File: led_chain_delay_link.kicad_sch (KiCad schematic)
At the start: 5 parts, among them Q2801 2N7002

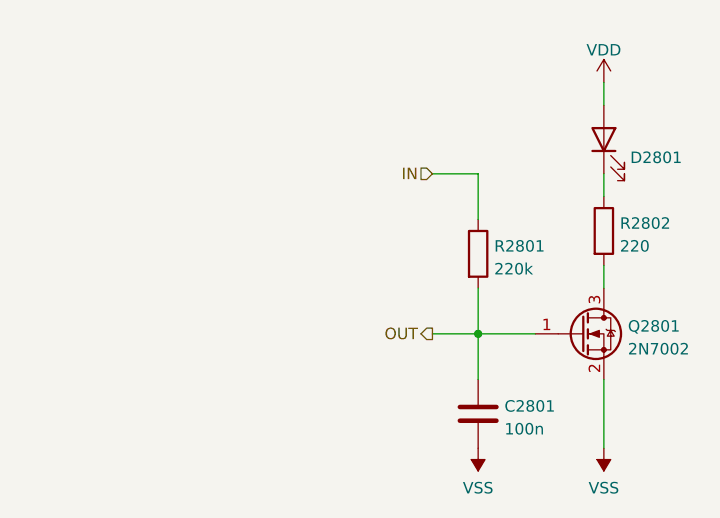
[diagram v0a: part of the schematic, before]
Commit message: sim for LED timings with gate in between
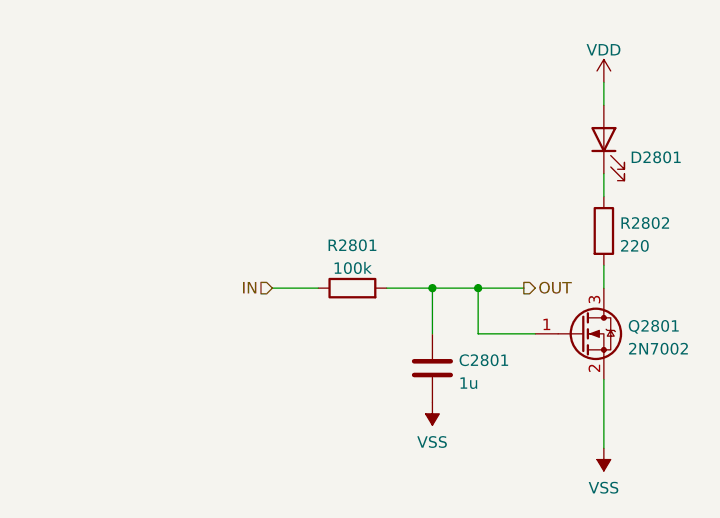
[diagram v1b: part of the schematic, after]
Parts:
- C2801: value 100n -> 1u; JLC C1525 -> C52923
- R2801: value 220k -> 100k; JLC C25767 -> C25741
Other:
- moved on the sheet: C2801, R2801
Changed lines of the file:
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@@
 (kicad_sch (version 20211123) (generator eeschema)
   (paper "A4")
-  (junction (at 146.05 172.72) (diameter 0) (color 0 0 0 0)
+  (junction (at 146.05 167.64) (diameter 0) (color 0 0 0 0)
+  )
+  (junction (at 140.97 167.64) (diameter 0) (color 0 0 0 0)
   )
   (wire (pts (xy 160.02 177.8) (xy 160.02 185.42))
+    (stroke (width 0) (type default) (color 0 0 0 0))
+  )
+  (wire (pts (xy 151.13 167.64) (xy 146.05 167.64))
+    (stroke (width 0) (type default) (color 0 0 0 0))
+  )
+  (wire (pts (xy 160.02 165.1) (xy 160.02 167.64))
     (stroke (width 0) (type default) (color 0 0 0 0))
   )
@@
     (stroke (width 0) (type default) (color 0 0 0 0))
   )
-  (wire (pts (xy 160.02 165.1) (xy 160.02 167.64))
+  (wire (pts (xy 160.02 144.78) (xy 160.02 147.32))
     (stroke (width 0) (type default) (color 0 0 0 0))
   )
-  (wire (pts (xy 160.02 144.78) (xy 160.02 147.32))
+  (wire (pts (xy 140.97 167.64) (xy 135.89 167.64))
     (stroke (width 0) (type default) (color 0 0 0 0))
   )
@@
     (stroke (width 0) (type default) (color 0 0 0 0))
   )
-  (wire (pts (xy 146.05 154.94) (xy 146.05 160.02))
+  (wire (pts (xy 146.05 167.64) (xy 140.97 167.64))
     (stroke (width 0) (type default) (color 0 0 0 0))
   )
-  (wire (pts (xy 140.97 172.72) (xy 146.05 172.72))
+  (wire (pts (xy 140.97 167.64) (xy 140.97 172.72))
     (stroke (width 0) (type default) (color 0 0 0 0))
   )
-  (wire (pts (xy 146.05 177.8) (xy 146.05 172.72))
-    (stroke (width 0) (type default) (color 0 0 0 0))
-  )
-  (wire (pts (xy 140.97 154.94) (xy 146.05 154.94))
+  (wire (pts (xy 123.19 167.64) (xy 128.27 167.64))
     (stroke (width 0) (type default) (color 0 0 0 0))
   )
@@
     (effects (font (size 2.54 2.54) (thickness 0.508) bold) (justify left bottom))
   )
-  (hierarchical_label "OUT" (shape output) (at 140.97 172.72 180)
+  (hierarchical_label "OUT" (shape output) (at 151.13 167.64 0)
+    (effects (font (size 1.27 1.27)) (justify left))
+  )
+  (hierarchical_label "IN" (shape input) (at 123.19 167.64 180)
     (effects (font (size 1.27 1.27)) (justify right))
   )
-  (hierarchical_label "IN" (shape input) (at 140.97 154.94 180)
-    (effects (font (size 1.27 1.27)) (justify right))
-  )
-  (symbol (lib_id "Device:R") (at 146.05 163.83 0) (unit 1)
+  (symbol (lib_id "Device:R") (at 132.08 167.64 90) (unit 1)
     (in_bom yes) (on_board yes) (fields_autoplaced)
-    (property "Reference" "R2801" (id 0) (at 147.828 162.9953 0)
-      (effects (font (size 1.27 1.27)) (justify left))
-    )
-    (property "Value" "220k" (id 1) (at 147.828 165.5322 0)
-      (effects (font (size 1.27 1.27)) (justify left))
-    )
-    (property "Footprint" "Resistor_SMD:R_0402_1005Metric" (id 2) (at 144.272 163.83 90)
+    (property "Reference" "R2801" (id 0) (at 132.08 162.9242 90))
+    (property "Value" "100k" (id 1) (at 132.08 165.4611 90))
+    (property "Footprint" "Resistor_SMD:R_0402_1005Metric" (id 2) (at 132.08 169.418 90)
       (effects (font (size 1.27 1.27)) hide)
     )
-    (property "Datasheet" "~" (id 3) (at 146.05 163.83 0)
+    (property "Datasheet" "~" (id 3) (at 132.08 167.64 0)
       (effects (font (size 1.27 1.27)) hide)
     )
-    (property "JLC" "C25767" (id 4) (at 146.05 163.83 90)
+    (property "JLC" "C25741" (id 4) (at 132.08 167.64 90)
       (effects (font (size 1.27 1.27)) hide)
     )
@@
     (pin "2")
   )
-  (symbol (lib_id "power:VSS") (at 146.05 185.42 180) (unit 1)
+  (symbol (lib_id "power:VSS") (at 140.97 180.34 180) (unit 1)
     (in_bom yes) (on_board yes) (fields_autoplaced)
-    (property "Reference" "#PWR02801" (id 0) (at 146.05 181.61 0)
+    (property "Reference" "#PWR02801" (id 0) (at 140.97 176.53 0)
       (effects (font (size 1.27 1.27)) hide)
     )
-    (property "Value" "VSS" (id 1) (at 146.05 189.8634 0))
-    (property "Footprint" "" (id 2) (at 146.05 185.42 0)
+    (property "Value" "VSS" (id 1) (at 140.97 184.7834 0))
+    (property "Footprint" "" (id 2) (at 140.97 180.34 0)
       (effects (font (size 1.27 1.27)) hide)
     )
-    (property "Datasheet" "" (id 3) (at 146.05 185.42 0)
+    (property "Datasheet" "" (id 3) (at 140.97 180.34 0)
       (effects (font (size 1.27 1.27)) hide)
     )
@@
     (pin "1")
   )
-  (symbol (lib_id "Device:C") (at 146.05 181.61 0) (unit 1)
+  (symbol (lib_id "Device:C") (at 140.97 176.53 0) (unit 1)
     (in_bom yes) (on_board yes) (fields_autoplaced)
-    (property "Reference" "C2801" (id 0) (at 148.971 180.7753 0)
+    (property "Reference" "C2801" (id 0) (at 143.891 175.6953 0)
       (effects (font (size 1.27 1.27)) (justify left))
     )
-    (property "Value" "100n" (id 1) (at 148.971 183.3122 0)
+    (property "Value" "1u" (id 1) (at 143.891 178.2322 0)
       (effects (font (size 1.27 1.27)) (justify left))
     )
-    (property "Footprint" "Capacitor_SMD:C_0402_1005Metric" (id 2) (at 147.0152 185.42 0)
+    (property "Footprint" "Capacitor_SMD:C_0402_1005Metric" (id 2) (at 141.9352 180.34 0)
       (effects (font (size 1.27 1.27)) hide)
     )
-    (property "Datasheet" "https://datasheet.lcsc.com/lcsc/1810191219_Samsung-Electro-Mechanics-CL05B104KO5NNNC_C1525.pdf" (id 3) (at 146.05 181.61 0)
+    (property "Datasheet" "https://datasheet.lcsc.com/lcsc/1810191219_Samsung-Electro-Mechanics-CL05B104KO5NNNC_C1525.pdf" (id 3) (at 140.97 176.53 0)
       (effects (font (size 1.27 1.27)) hide)
     )
-    (property "JLC" "C1525" (id 4) (at 146.05 181.61 0)
+    (property "JLC" "C52923" (id 4) (at 140.97 176.53 0)
       (effects (font (size 1.27 1.27)) hide)
     )
